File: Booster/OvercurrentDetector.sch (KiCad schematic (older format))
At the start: 38 parts

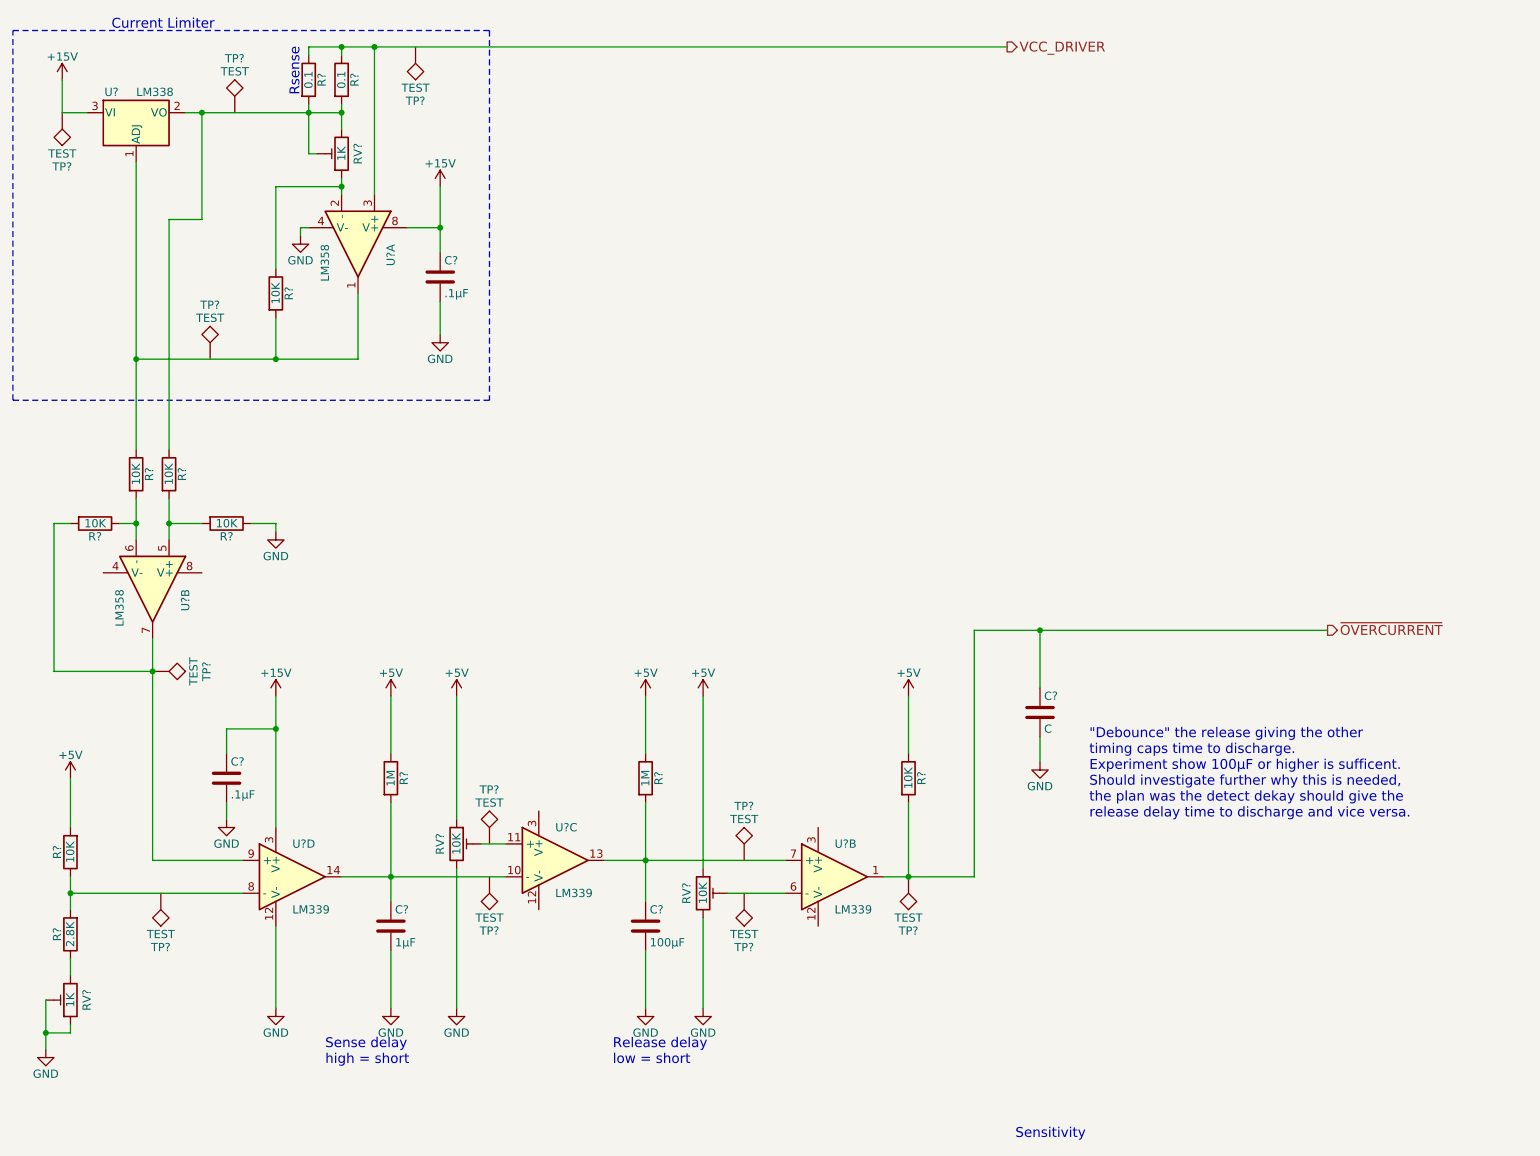
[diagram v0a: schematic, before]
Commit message: Kind of working with the overcurrent retry, but not liking the RC delay in the final output to the motor driver.
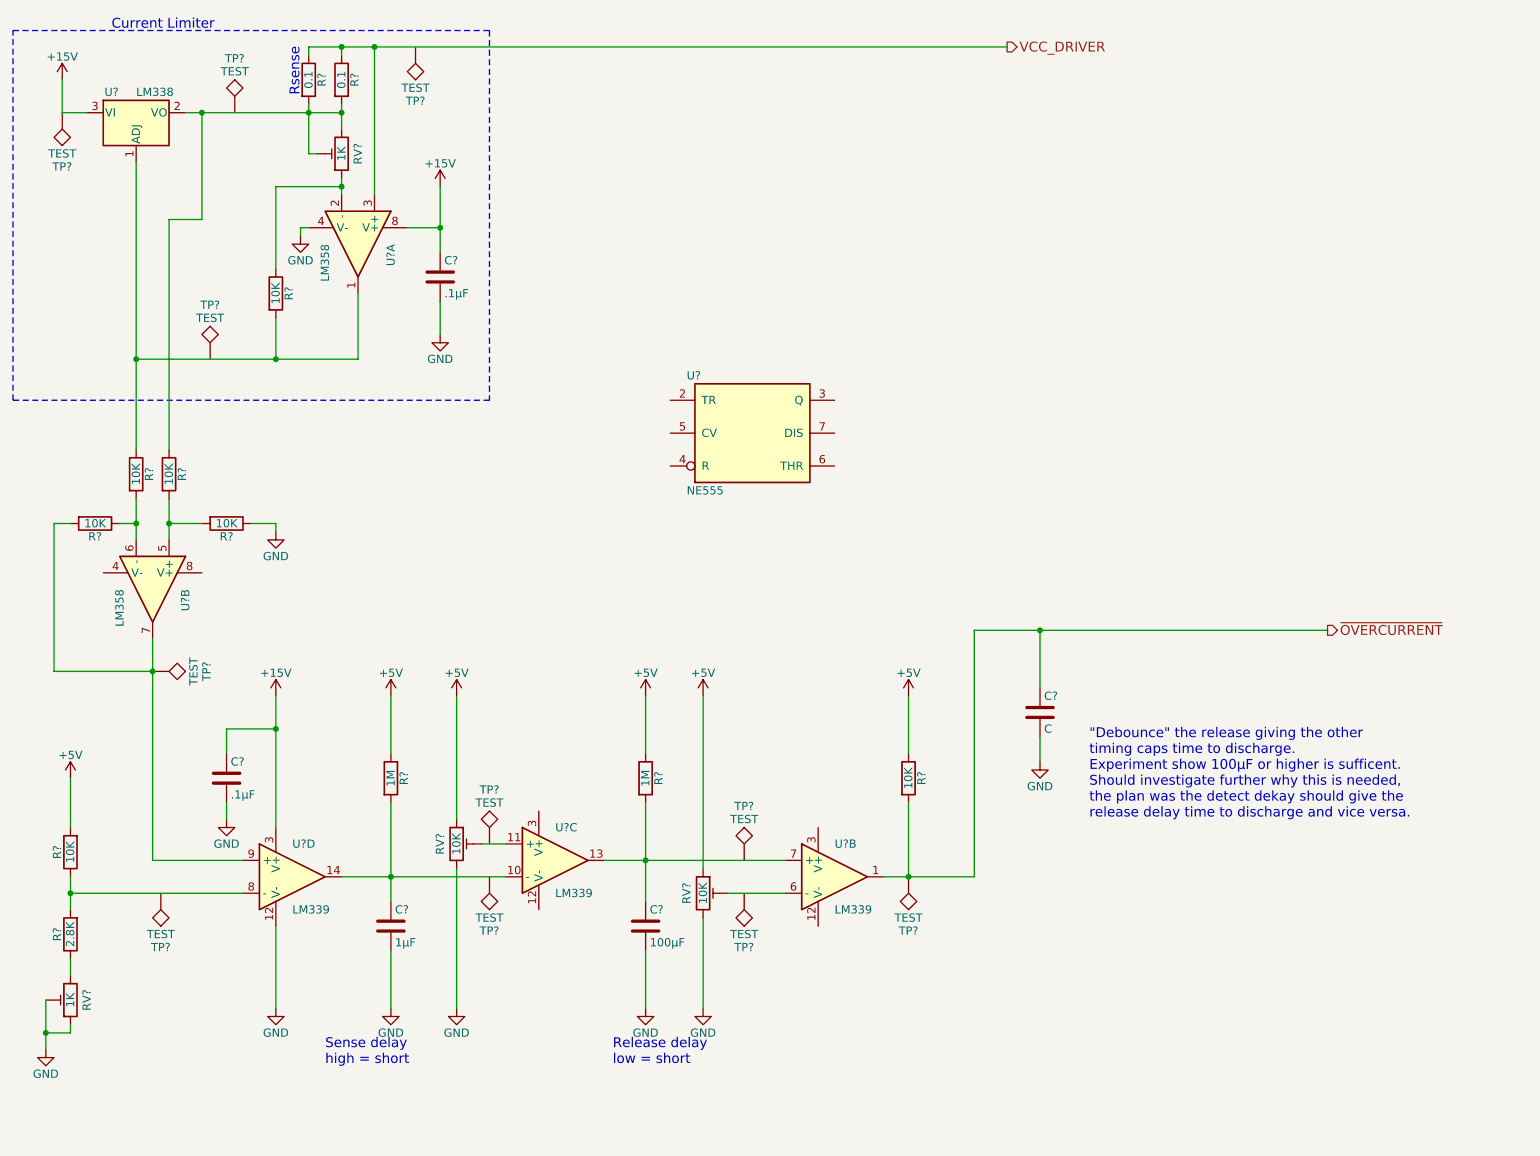
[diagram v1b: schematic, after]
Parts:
- added U?: NE555, symbol NE555
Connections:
- net GND: now also U?.1 (GND)
- new net VCC: U?.8 (VCC)
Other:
- note removed: "Sensitivity"

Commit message: Added 555 timer to control overcurrent release delay. Simpler to control as turning the power off cleared the overflow before the capacitor controlling the release delay was fully cleared. The LM339 is still doing the detect delay.
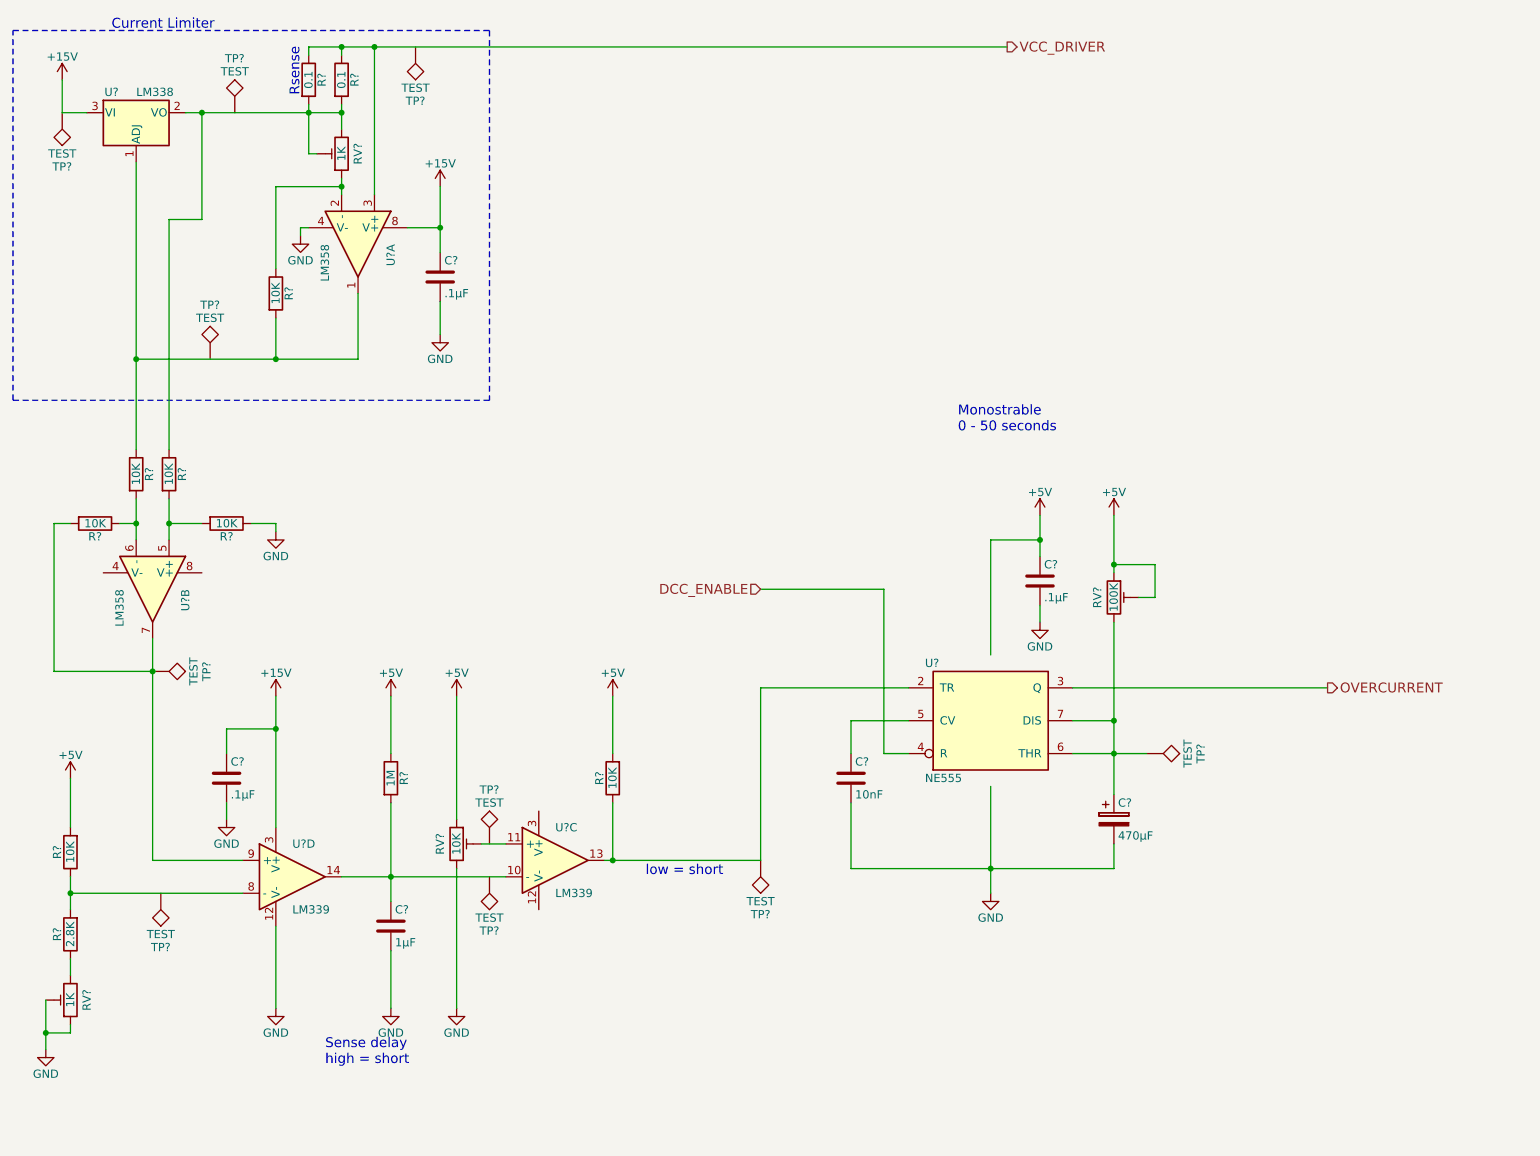
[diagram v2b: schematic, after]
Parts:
- removed C?: 100µF, symbol C
- removed C?: C, symbol C
- removed R?: 1M, symbol R
- removed R?: 10K, symbol R
- removed RV?: 10K, symbol POT_TRIM
- removed TP? (x3): TEST, symbol TEST
- removed U?: LM339, symbol LM339
- added C?: 10nF, symbol C
- added C?: .1µF, symbol C
- added C?: 470µF, symbol CP
- added R?: 10K, symbol R
- added RV?: 100K, symbol POT_TRIM
- added TP? (x2): TEST, symbol TEST
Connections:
- net VCC is gone; now on net +5V: U?.8 (VCC)
- net +5V: now also C?.1, R?.2, RV?.1, RV?.2
- net GND: now also C?.2, C?.2, C?.2
- net at U?.13: now also U?.2 (TR), R?.1, TP?.1
- net OVERCURRENT: now reaches U?.3 (Q)
- net DCC_ENABLE: now reaches U?.4 (R)
- net at U?.5 (CV): now also C?.1
- net at U?.6 (THR): now also U?.7 (DIS), C?.1, RV?.3, TP?.1
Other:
- note added: "Monostrable\n0 - 50 seconds"
- note added: "low = short"
- note removed: ""Debounce" the release giving the other\ntiming caps time to discharge.\nExperiment show 100µF or higher is sufficent.\nShould investigate further why this is needed,\nthe plan was the detect dekay should give the\nrelease delay time to discharge and vice versa."
- note removed: "Release delay\nlow = short"
- moved on the sheet: U?

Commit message: Reset overcurrent timeout now linked to the master switch, not the input signal.
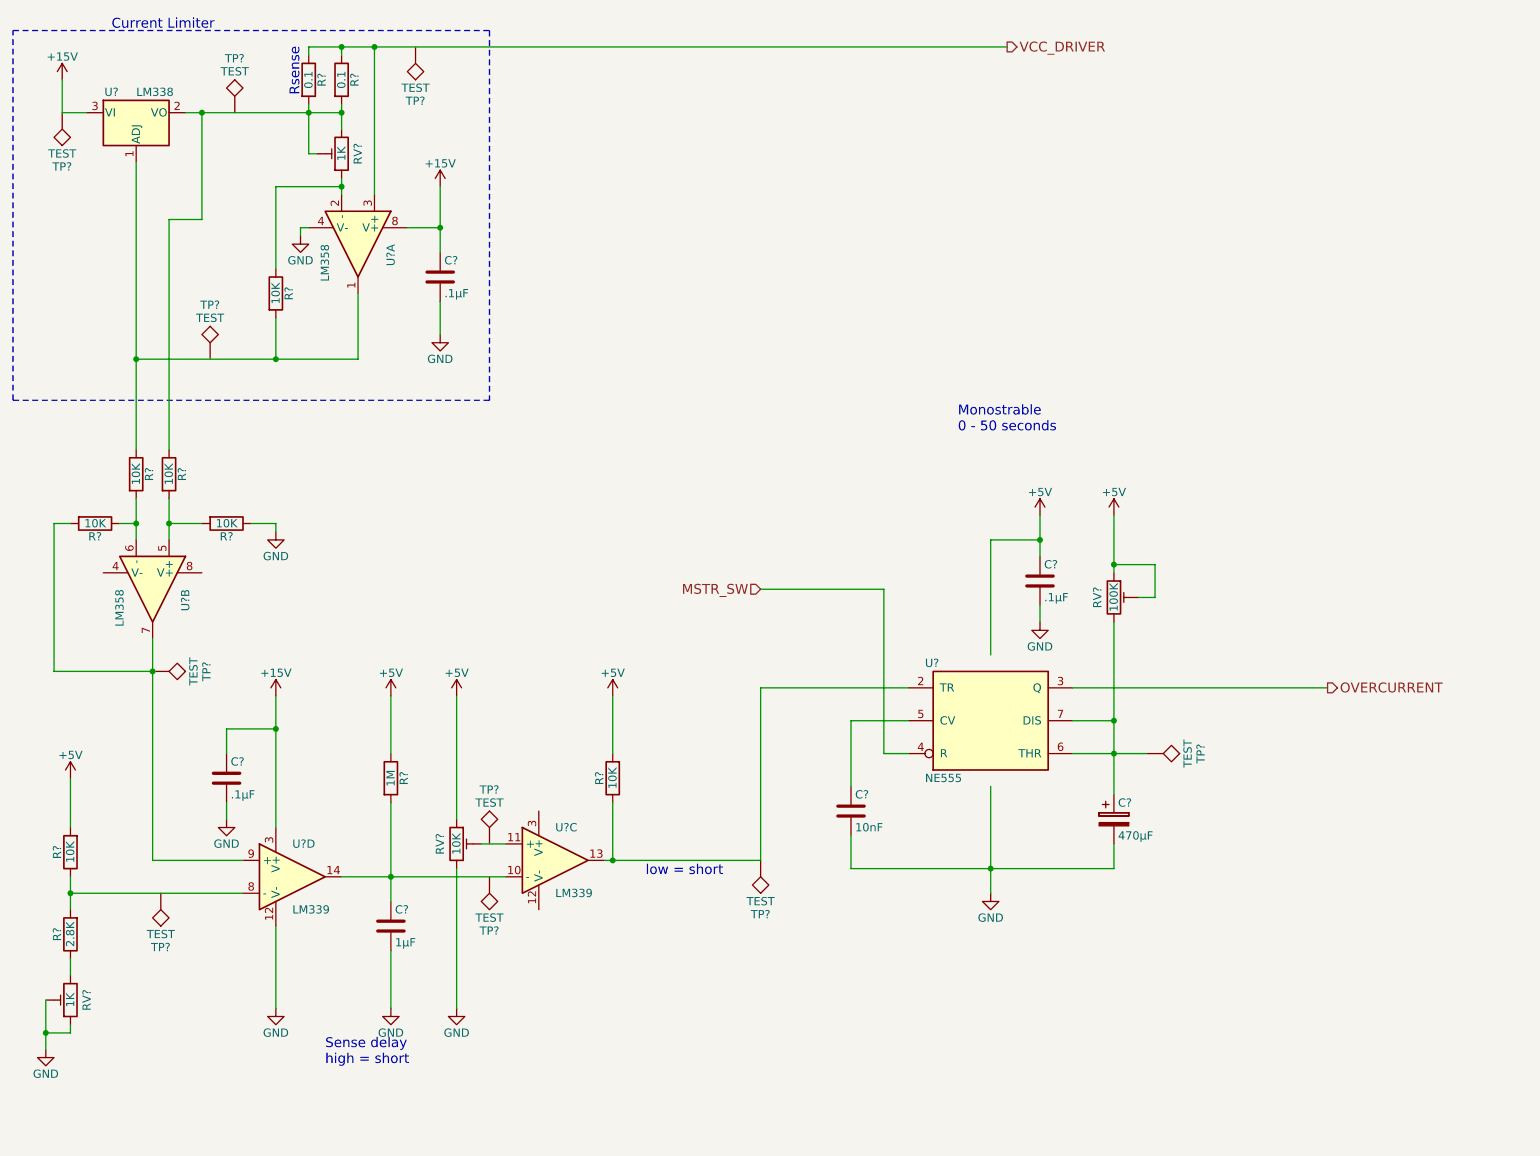
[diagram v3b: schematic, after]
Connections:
- net DCC_ENABLE renamed MSTR_SW
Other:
- moved on the sheet: C?
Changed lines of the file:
@@
 L C C?
 U 1 1 5A36BBC1
-P 7400 5450
-F 0 "C?" H 7425 5550 50  0000 L CNN
-F 1 "10nF" H 7425 5350 50  0000 L CNN
-F 2 "" H 7438 5300 50  0001 C CNN
-F 3 "" H 7400 5450 50  0001 C CNN
-	1    7400 5450
+P 7400 5650
+F 0 "C?" H 7425 5750 50  0000 L CNN
+F 1 "10nF" H 7425 5550 50  0000 L CNN
+F 2 "" H 7438 5500 50  0001 C CNN
+F 3 "" H 7400 5650 50  0001 C CNN
+	1    7400 5650
 	1    0    0    -1
 $EndComp
@@
 Connection ~ 2650 6150
 Wire Wire Line
-	2650 6050 2650 6250
+	2650 6050 2650 6150
+Wire Wire Line
+	2650 6150 2650 6250
 Wire Wire Line
 	2750 1400 2600 1400
@@
 	2600 1400 2600 1200
 Wire Wire Line
-	3050 2900 4400 2900
-Wire Wire Line
-	4100 1350 4100 1650
+	3050 2900 3900 2900
+Wire Wire Line
+	3900 2900 4400 2900
+Wire Wire Line
+	4100 1350 4100 1400
+Wire Wire Line
+	4100 1400 4100 1650
 Wire Wire Line
 	4100 1050 4100 1000
 Wire Wire Line
-	4100 1000 8350 1000
+	4100 1000 4300 1000
+Wire Wire Line
+	4300 1000 4500 1000
+Wire Wire Line
+	4500 1000 8350 1000
 Wire Wire Line
 	4300 1000 4300 1050
@@
 	4100 1650 4150 1650
 Wire Wire Line
-	4300 1350 4300 1500
-Wire Wire Line
-	4300 1800 4300 1900
-Wire Wire Line
-	3350 1400 4300 1400
+	4300 1350 4300 1400
+Wire Wire Line
+	4300 1400 4300 1500
+Wire Wire Line
+	4300 1800 4300 1850
+Wire Wire Line
+	4300 1850 4300 1900
+Wire Wire Line
+	3350 1400 3450 1400
+Wire Wire Line
+	3450 1400 4100 1400
+Wire Wire Line
+	4100 1400 4300 1400
 Wire Wire Line
 	4500 1000 4500 1900
@@
 	4700 2100 4900 2100
 Wire Wire Line
-	4900 1850 4900 2250
+	4900 1850 4900 2100
+Wire Wire Line
+	4900 2100 4900 2250
 Connection ~ 4900 2100
 Wire Wire Line
 	4900 2750 4900 2550
 Wire Wire Line
-	3050 1700 3050 3450
-Wire Wire Line
-	3050 3750 3050 4000
-Wire Wire Line
-	3250 3750 3250 4000
+	3050 1700 3050 2900
+Wire Wire Line
+	3050 2900 3050 3450
+Wire Wire Line
+	3050 3750 3050 3900
+Wire Wire Line
+	3050 3900 3050 4000
+Wire Wire Line
+	3250 3750 3250 3900
+Wire Wire Line
+	3250 3900 3250 4000
 Wire Wire Line
 	3250 2050 3250 3450
@@
 	2650 5750 2650 5450
 Wire Wire Line
-	2500 6800 2500 7100
+	2500 6800 2500 7000
+Wire Wire Line
+	2500 7000 2500 7100
 Wire Wire Line
 	2650 6650 2650 6550
@@
 Connection ~ 3150 4800
 Wire Wire Line
-	4300 6050 5300 6050
-Wire Wire Line
-	4600 5600 4600 6200
+	4300 6050 4600 6050
+Wire Wire Line
+	4600 6050 5300 6050
+Wire Wire Line
+	4600 5600 4600 6050
+Wire Wire Line
+	4600 6050 4600 6200
 Connection ~ 4600 6050
 Wire Wire Line
@@
 	4600 6500 4600 6850
 Wire Wire Line
-	3150 4600 3150 5950
+	3150 4600 3150 4800
+Wire Wire Line
+	3150 4800 3150 5950
 Wire Wire Line
 	3150 5950 3700 5950
@@
 	3600 5700 3600 5600
 Wire Wire Line
-	3900 4950 3900 5750
+	3900 4950 3900 5150
+Wire Wire Line
+	3900 5150 3900 5750
 Wire Wire Line
 	3600 5300 3600 5150
@@
 	3900 6350 3900 6850
 Wire Wire Line
-	5900 5950 6850 5950
+	5900 5950 5950 5950
+Wire Wire Line
+	5950 5950 6850 5950
 Wire Wire Line
 	6850 5950 6850 4900
@@
 	7750 5100 7400 5100
 Wire Wire Line
-	7400 5100 7400 5300
+	7400 5100 7400 5500
 Wire Wire Line
 	8250 4700 8250 4000
@@
 	8250 4000 8550 4000
 Wire Wire Line
-	8550 3850 8550 4100
+	8550 3850 8550 4000
+Wire Wire Line
+	8550 4000 8550 4100
 Connection ~ 8550 4000
 Wire Wire Line
@@
 	8750 5100 9000 5100
 Wire Wire Line
-	9000 4500 9000 5550
-Wire Wire Line
-	8750 5300 9200 5300
+	9000 4500 9000 5100
+Wire Wire Line
+	9000 5100 9000 5300
+Wire Wire Line
+	9000 5300 9000 5550
+Wire Wire Line
+	8750 5300 9000 5300
+Wire Wire Line
+	9000 5300 9200 5300
 Connection ~ 9000 5300
 Connection ~ 9000 5100
@@
 	9250 4150 9000 4150
 Wire Wire Line
-	9000 3850 9000 4200
+	9000 3850 9000 4150
+Wire Wire Line
+	9000 4150 9000 4200
 Connection ~ 9000 4150
 Wire Wire Line
-	7400 5600 7400 6000
-Wire Wire Line
-	7400 6000 9000 6000
-Wire Wire Line
-	8250 5500 8250 6150
+	7400 5800 7400 6000
+Wire Wire Line
+	7400 6000 8250 6000
+Wire Wire Line
+	8250 6000 9000 6000
+Wire Wire Line
+	8250 5500 8250 6000
+Wire Wire Line
+	8250 6000 8250 6150
 Connection ~ 8250 6000
 $Comp
@@
 $EndComp
 Text HLabel 6850 4300 0    60   Input ~ 0
-DCC_ENABLE
+MSTR_SW
 Wire Wire Line
 	7600 4300 6850 4300
